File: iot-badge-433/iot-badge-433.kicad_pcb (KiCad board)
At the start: 2 copper layers, 70 x 100 mm, 64 parts, among them J1 USB_C_Receptacle_USB2.0, J2 Wire ANT, Q1 BC847, Q2 BC847, Q3 BC847, SW1 SW_Push, SW2 SW_Push, SW3 SW_Push, SW4 SW_Push, SW5 SW_Push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

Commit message: 433 gerbers ok
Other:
- board text added: "IoT Badge V 00 433"
- board text removed: "IoT Badge V 00"
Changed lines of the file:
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@@
   (gr_arc (start 100 52) (mid 100.585786 50.585786) (end 102 50) (layer "Edge.Cuts") (width 0.05))
   (gr_line (start 151 52.5) (end 151 55) (layer "Edge.Cuts") (width 0.05))
-  (gr_text "IoT Badge\nV 00" (at 104.14 144.78) (layer "B.SilkS")
+  (gr_text "IoT Badge\nV 00 433" (at 103.7 144.78) (layer "B.SilkS")
     (effects (font (size 0.8 0.8) (thickness 0.15)) (justify mirror))
   )
@@
     (effects (font (size 0.6 0.6) (thickness 0.15)))
   )
-  (gr_text "IoT Badge\nV 00" (at 104.14 147.32) (layer "F.SilkS")
+  (gr_text "IoT Badge\nV 00 433" (at 103.7 147.32) (layer "F.SilkS")
     (effects (font (size 0.8 0.8) (thickness 0.15)))
   )

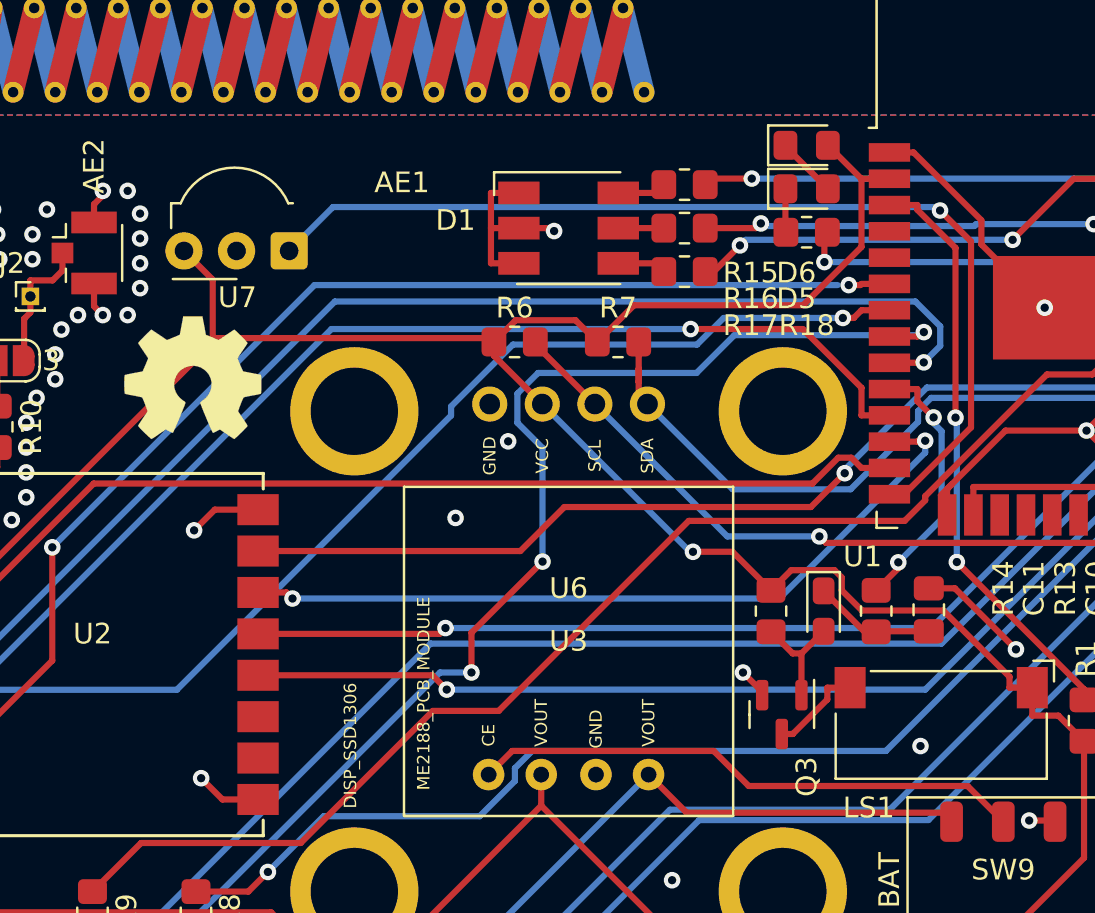
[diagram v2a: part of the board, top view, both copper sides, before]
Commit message: changed ir leds polarity, PSU silk and bypass jumper
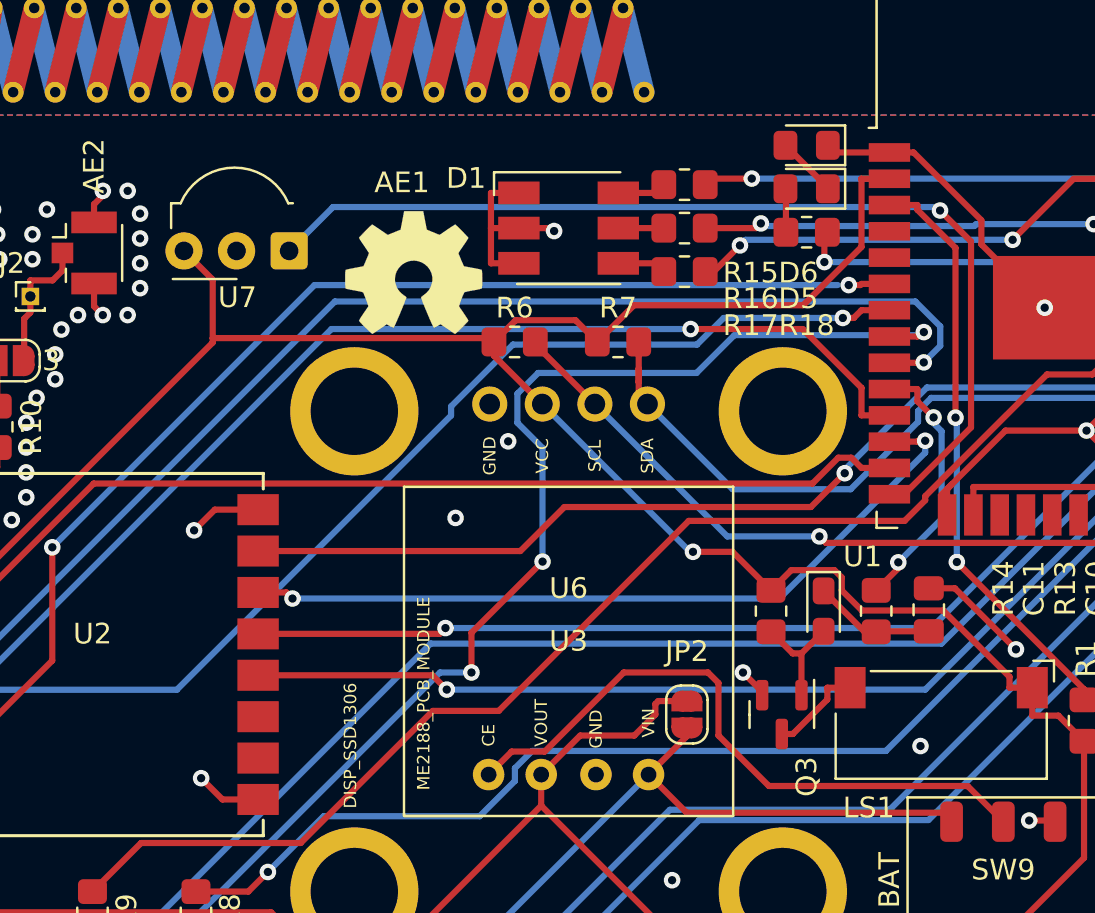
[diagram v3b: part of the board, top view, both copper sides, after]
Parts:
- added JP2: SolderJumper_2_Open, Jumper:SolderJumper-2_P1.3mm_Open_RoundedPad1.0x1.5mm, F.Cu at (140.7, 95.0)
- moved SYMB2 11.8 mm to (127.5, 73.7)
- turned D5 to 180 degrees
- turned D6 to 180 degrees
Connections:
- D6 pad 1: Net-(D5-Pad2) -> Earth
- D6 pad 2: +3V3 -> Net-(D5-Pad1)
- R18 pad 1: Net-(D5-Pad1) -> Net-(D5-Pad2)
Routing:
- net Net-(R11-Pad2): track 58.8 -> 67.6 mm
- net Net-(SW9-Pad5): track 26.8 -> 31.4 mm
- net Earth: track 199.7 -> 202.8 mm
- net +BATT: track 53.9 -> 56.9 mm
- net +3V3: track 115.2 -> 113.0 mm
- net Net-(D5-Pad1): track 2.11 -> 3.00 mm
- net Net-(D5-Pad2): track 2.95 -> 2.15 mm
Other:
- board text added: "VIN"

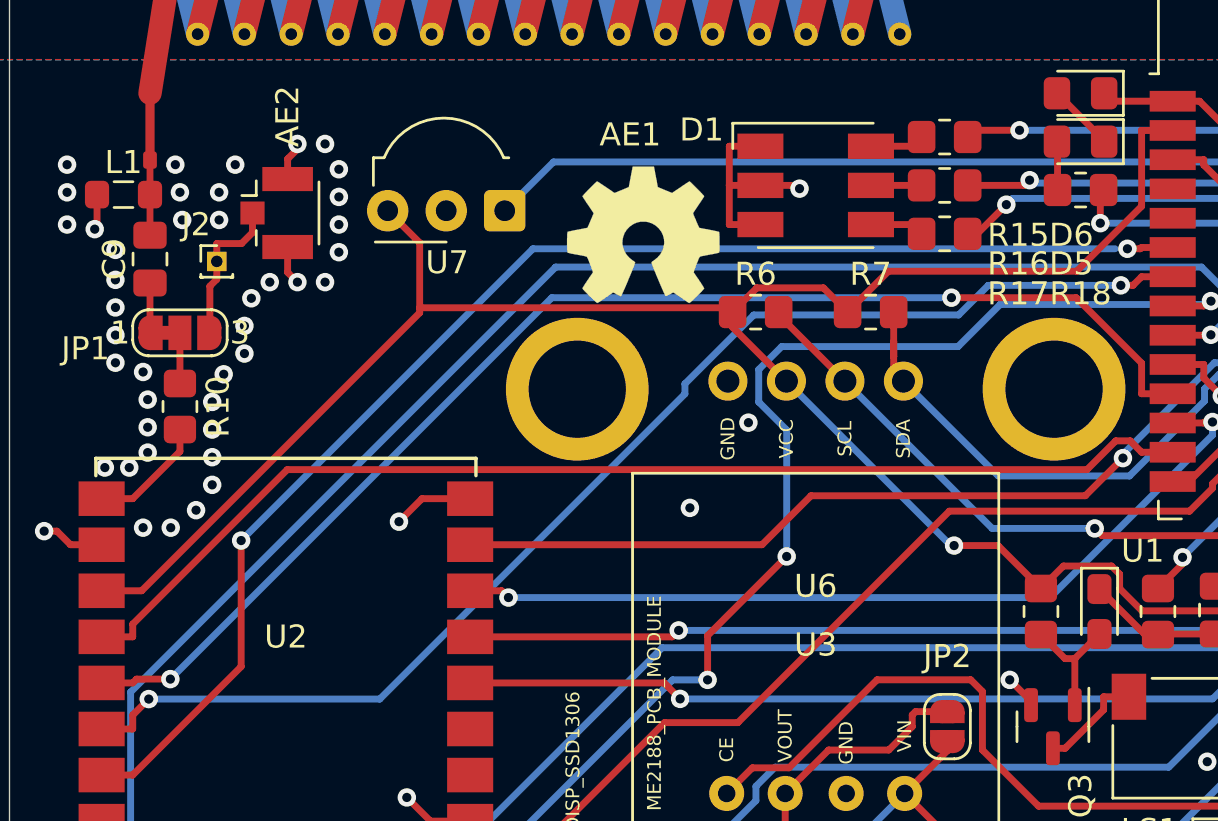
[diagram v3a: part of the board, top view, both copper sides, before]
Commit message: added external i2c pins
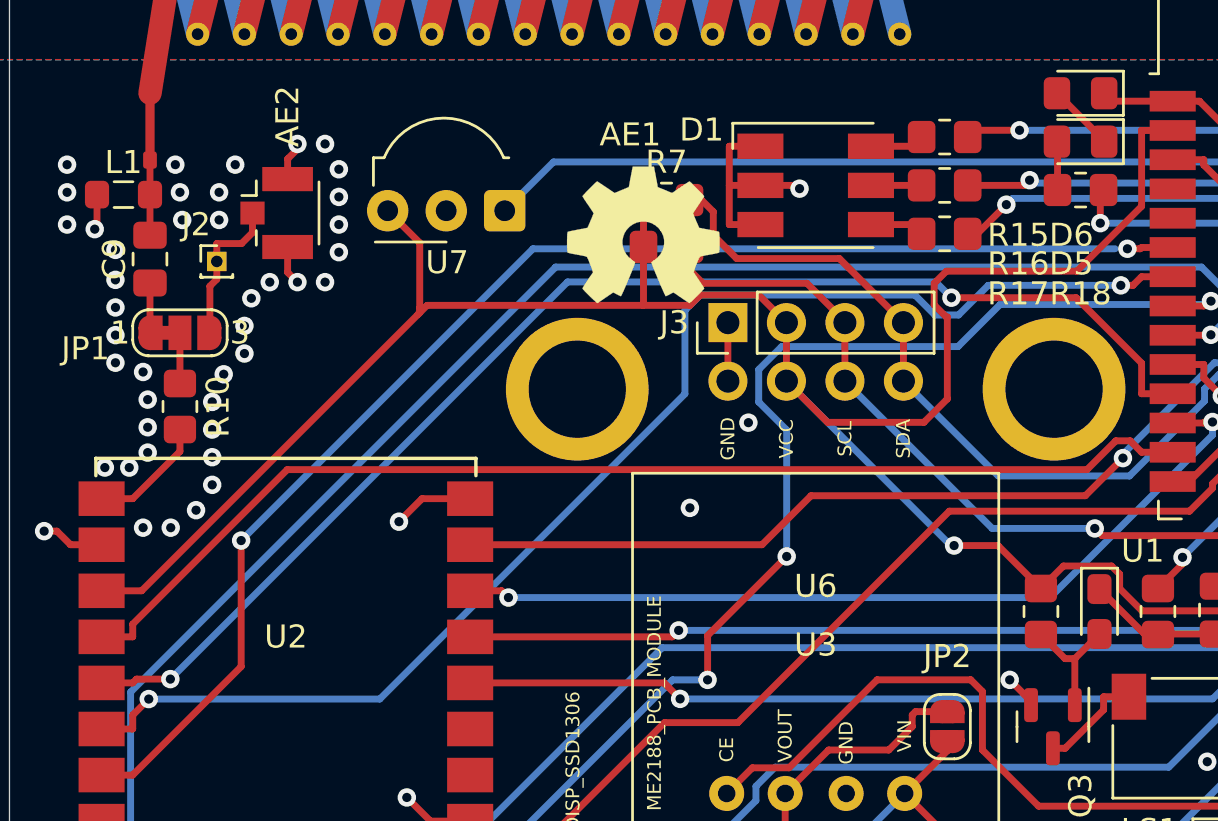
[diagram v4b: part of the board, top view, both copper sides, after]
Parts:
- added J3: Conn_01x04_Male, Connector_PinHeader_2.54mm:PinHeader_1x04_P2.54mm_Vertical, F.Cu at (131.2, 77.5)
- moved R7 10.1 mm to (128.5, 72.1)
- moved R6 4.79 mm to (128.5, 74.2)
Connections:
- net Net-(R6-Pad2) renamed /SCL
- net Net-(R7-Pad2) renamed /SDA
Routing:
- net /SDA: track 39.4 -> 51.4 mm
- net +3V3: track 113.0 -> 122.2 mm
- net /SCL: track 35.6 -> 42.0 mm
- net Net-(U1-Pad7): track 55.2 -> 57.8 mm
- net Earth: track 202.8 -> 205.0 mm
- net Net-(U1-Pad11): track 55.9 -> 56.5 mm

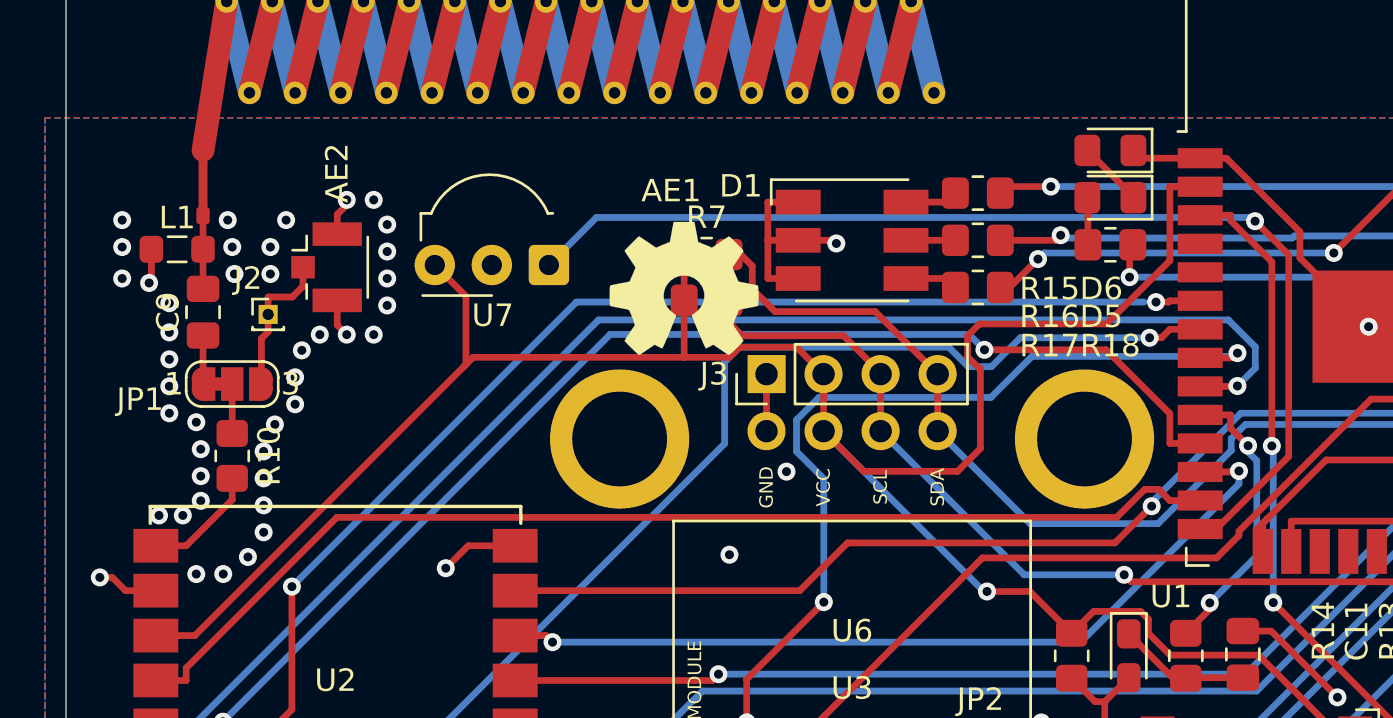
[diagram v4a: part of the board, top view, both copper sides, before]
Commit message: shifted ant match elements to the left
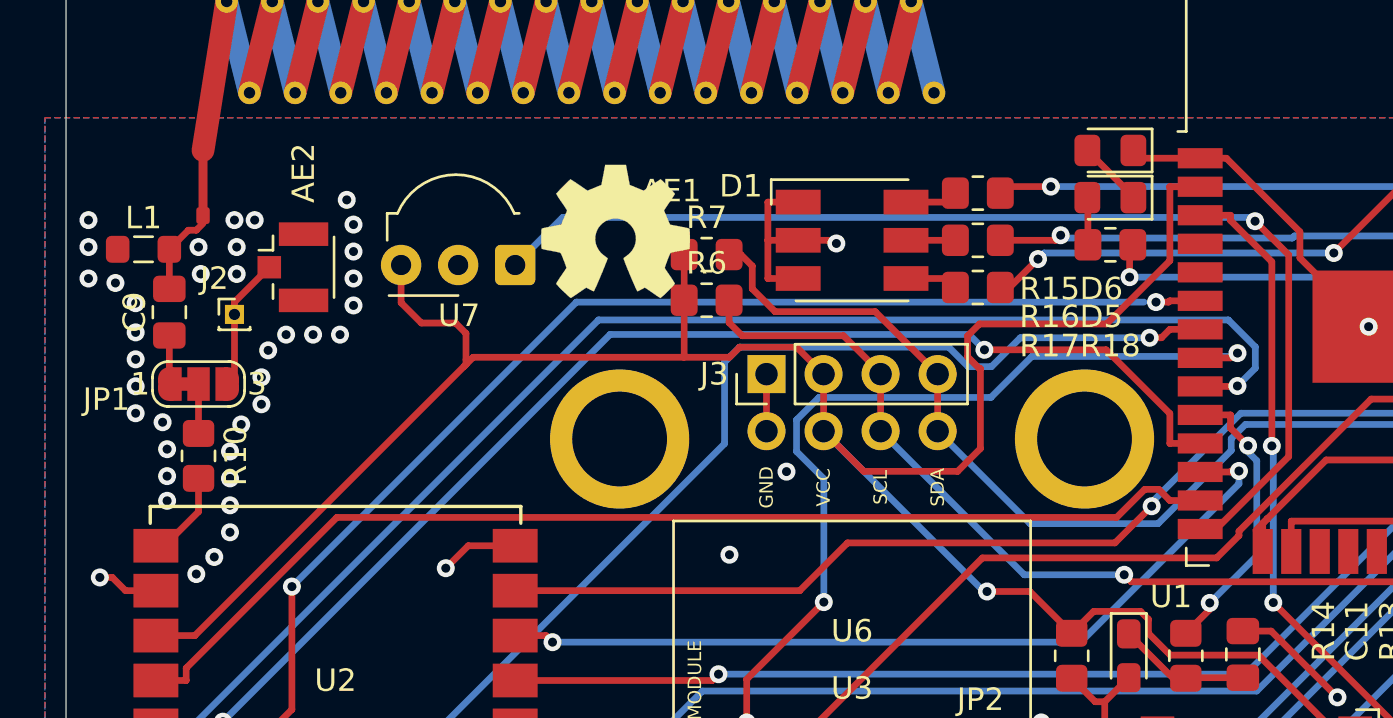
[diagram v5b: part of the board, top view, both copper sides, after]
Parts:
- moved SYMB2 3.97 mm to (124.5, 71.1)
- moved AE2 1.50 mm to (110.1, 72.7)
- moved C9 1.50 mm to (104.6, 74.7)
- moved J2 1.50 mm to (107.5, 74.8)
- moved JP1 1.50 mm to (105.9, 77.9)
- moved L1 1.50 mm to (103.5, 71.9)
- moved R10 1.50 mm to (105.9, 81.1)
- moved U7 1.50 mm to (120.0, 72.6)
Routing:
- net Earth: track 205.0 -> 200.3 mm, vias 96 -> 92
- net +3V3: track 122.2 -> 123.7 mm
- net /IRDEC-12: track 48.8 -> 50.3 mm
- net Net-(R10-Pad2): track 5.20 -> 4.01 mm
- net Net-(AE2-Pad1): track 6.60 -> 5.97 mm

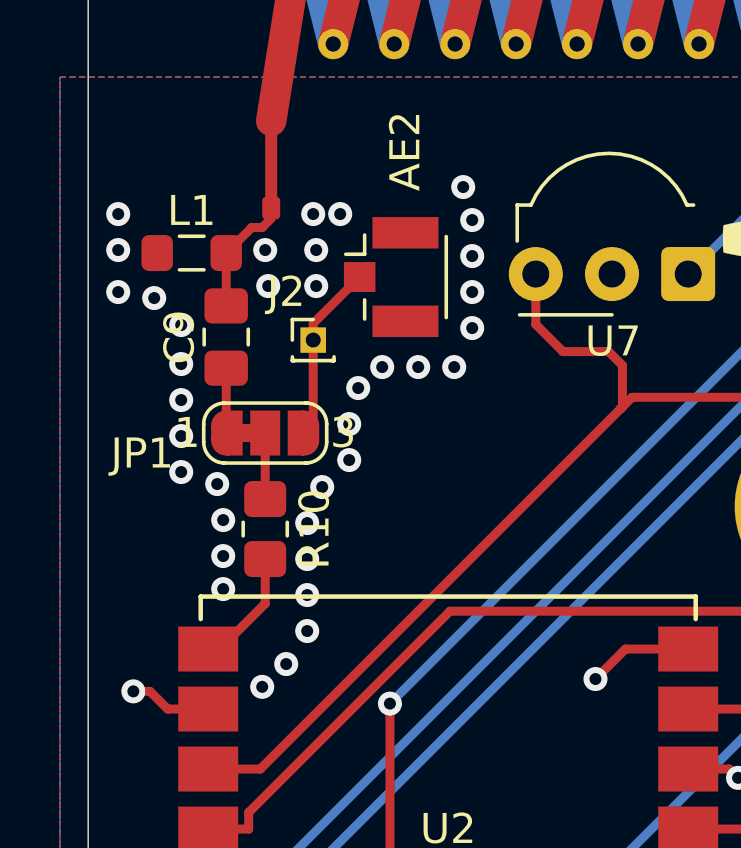
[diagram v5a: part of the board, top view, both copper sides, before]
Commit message: added tuning cap an inductor to ant circuit
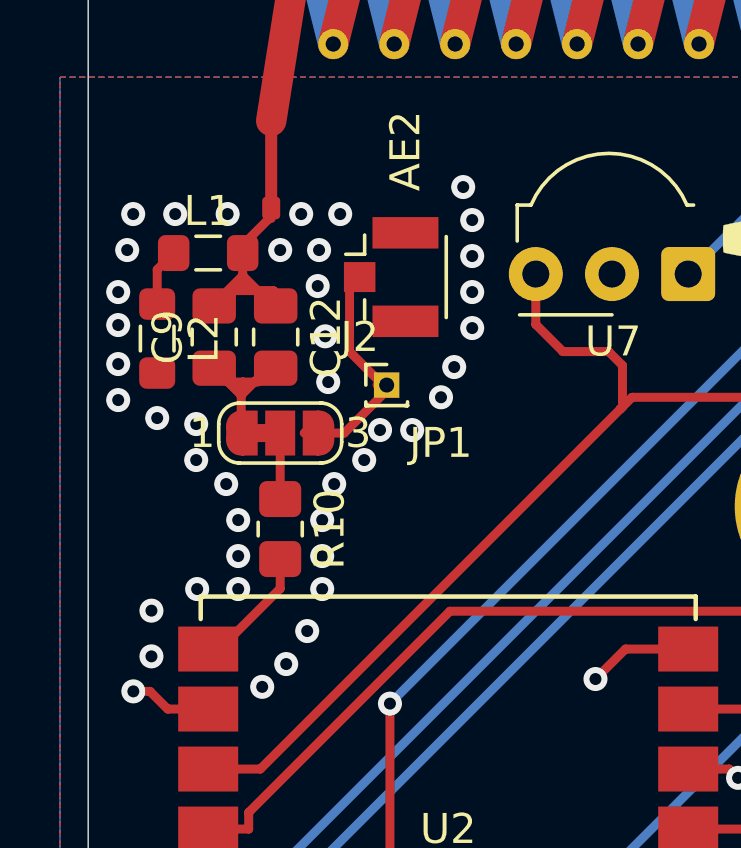
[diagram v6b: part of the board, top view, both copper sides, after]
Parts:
- added C12: C, Capacitor_SMD:C_0805_2012Metric_Pad1.18x1.45mm_HandSolder, F.Cu at (106.2, 74.7)
- added L2: L, Inductor_SMD:L_0805_2012Metric_Pad1.05x1.20mm_HandSolder, F.Cu at (102.3, 74.8)
- moved J2 2.87 mm to (110.0, 76.3)
- moved L1 0.55 mm to (104.0, 71.9)
- moved JP1 0.50 mm to (106.4, 77.9)
- moved R10 0.50 mm to (106.4, 81.1)
- moved C9 0.40 mm to (104.2, 74.7)
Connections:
- L1 pad 2: Earth -> Net-(L1-Pad2)
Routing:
- net Net-(AE1-Pad1): track 3.74 -> 8.49 mm
- net Net-(C9-Pad2): track 2.16 -> 6.17 mm
- net Net-(AE2-Pad1): track 5.97 -> 8.27 mm
- net Net-(L1-Pad2): track 0.00 -> 1.93 mm
- net Earth: vias 92 -> 97

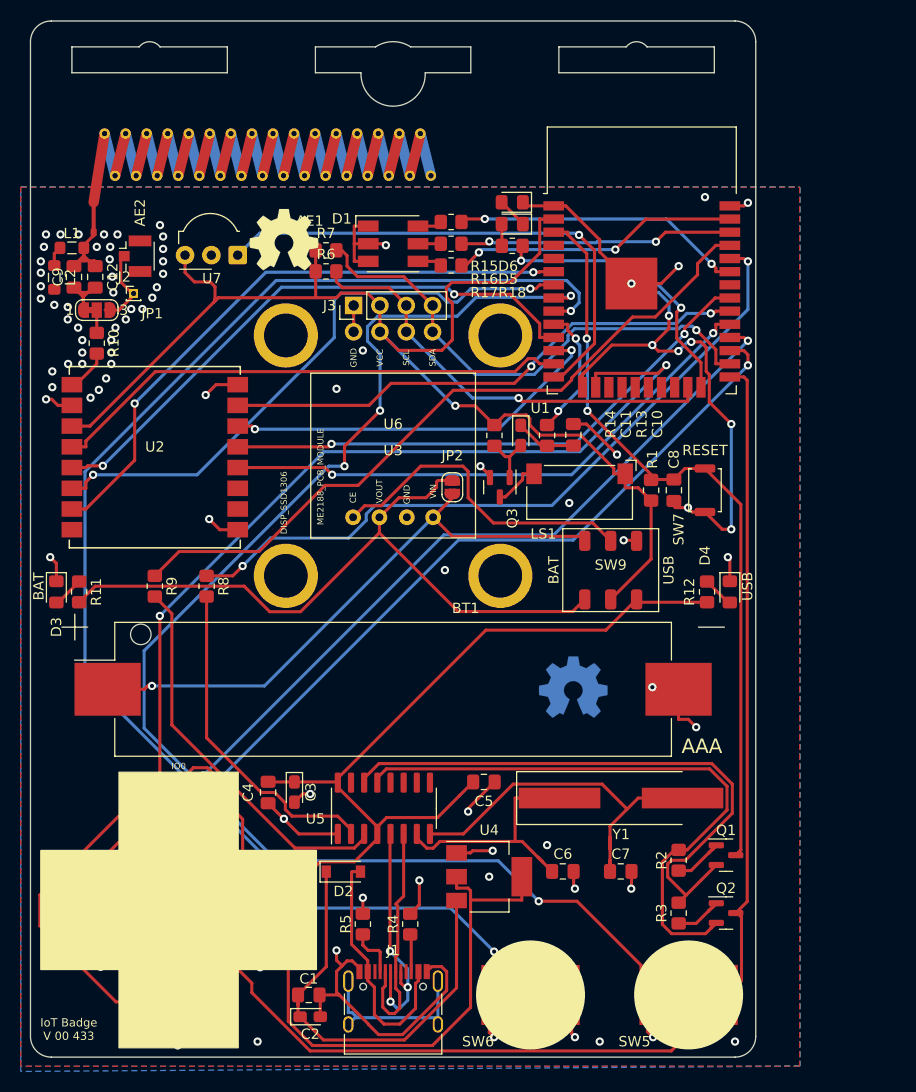
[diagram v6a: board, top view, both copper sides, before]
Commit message: enlarged AAA bat footprint pads
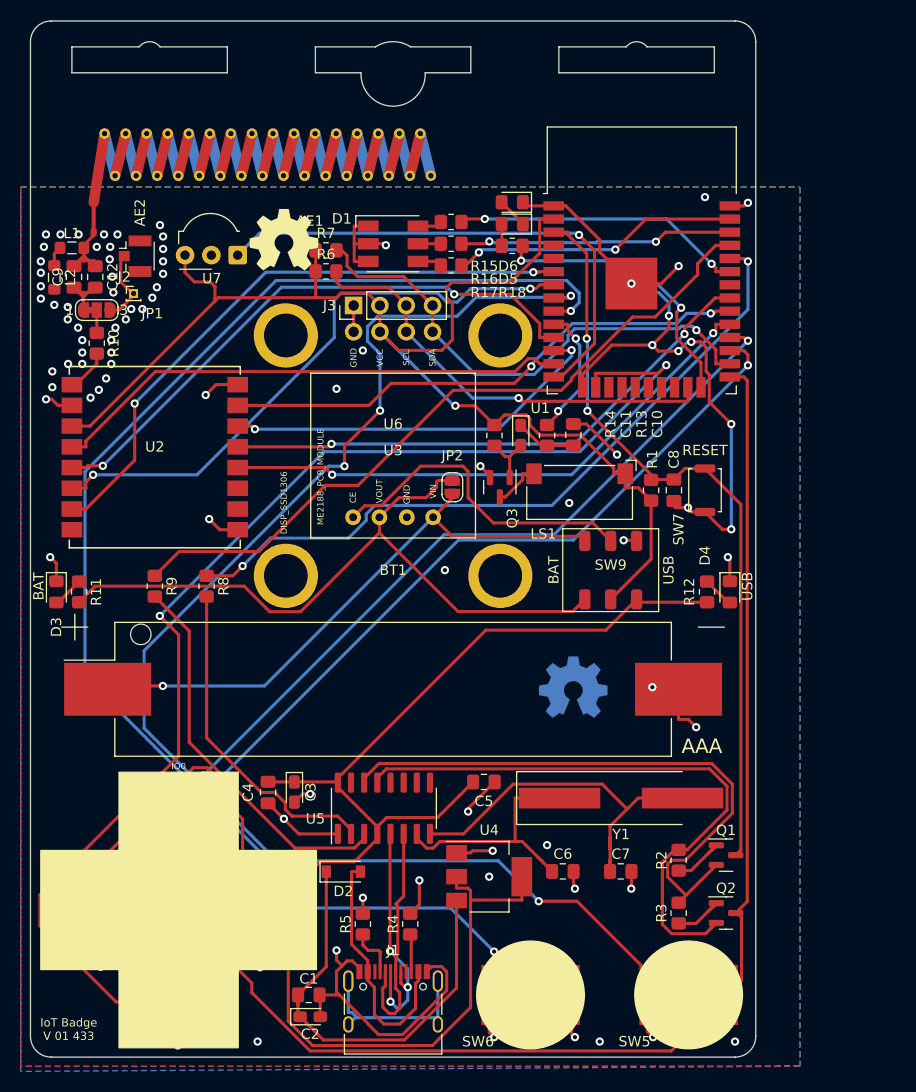
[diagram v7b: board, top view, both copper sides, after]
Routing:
- net /SW2-13: track 123.0 -> 124.5 mm
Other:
- board text added: "IoT Badge V 01 433"
- board text removed: "IoT Badge V 00 433"
